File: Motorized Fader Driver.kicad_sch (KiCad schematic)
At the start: 5 parts, among them J1 Conn_01x02, U1 DRV8833PWP, U2 RP2040

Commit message: Update PCB
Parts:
- removed U2: RP2040, Package_DFN_QFN:QFN-56-1EP_7x7mm_P0.4mm_EP3.2x3.2mm, symbol MCU_RaspberryPi:RP2040
- J1: footprint (none) -> Connector_PinHeader_2.54mm:PinHeader_1x02_P2.54mm_Vertical
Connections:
- net RP2040/GPIO5: now reaches U1.15 (AIN2)
- net RP2040/GPIO4: now reaches U1.16 (AIN1)
- net RP2040/GPIO6: now reaches R1.1, VR1.T1
- net RP2040/ADC0: now reaches VR1.B2 (WIPER_2)
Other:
- added sheet RP2040 (rp2040.kicad_sch)
- moved on the sheet: J1, R1, U1, VR1

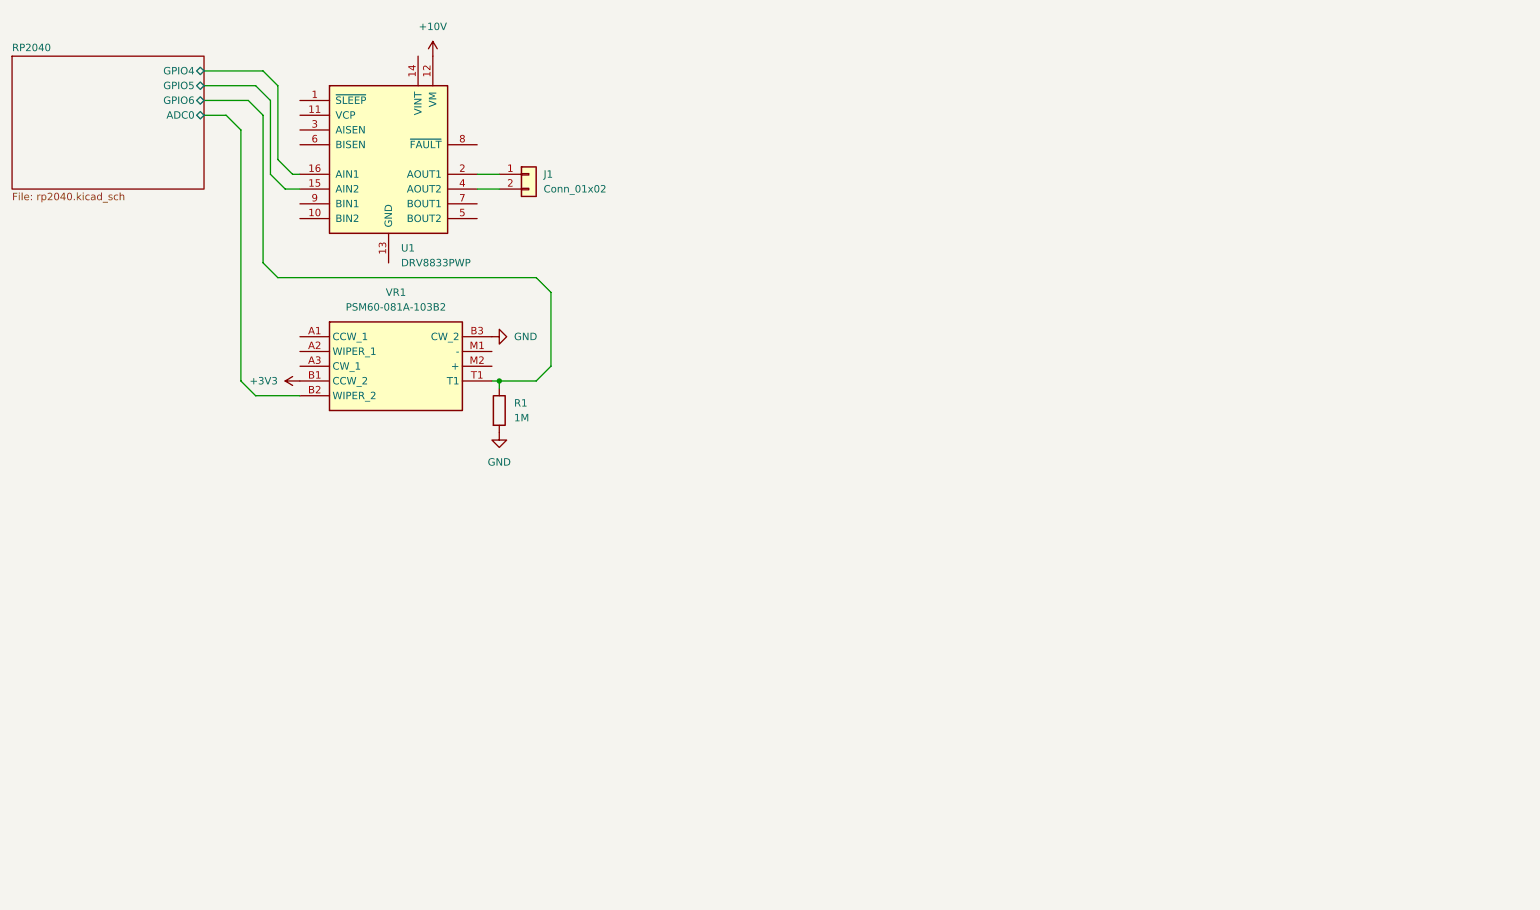
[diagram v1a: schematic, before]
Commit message: Finish most of the schematic design
The majority of the schematic is in a pretty finalized state now. Also
some more work on the PCB has been done.
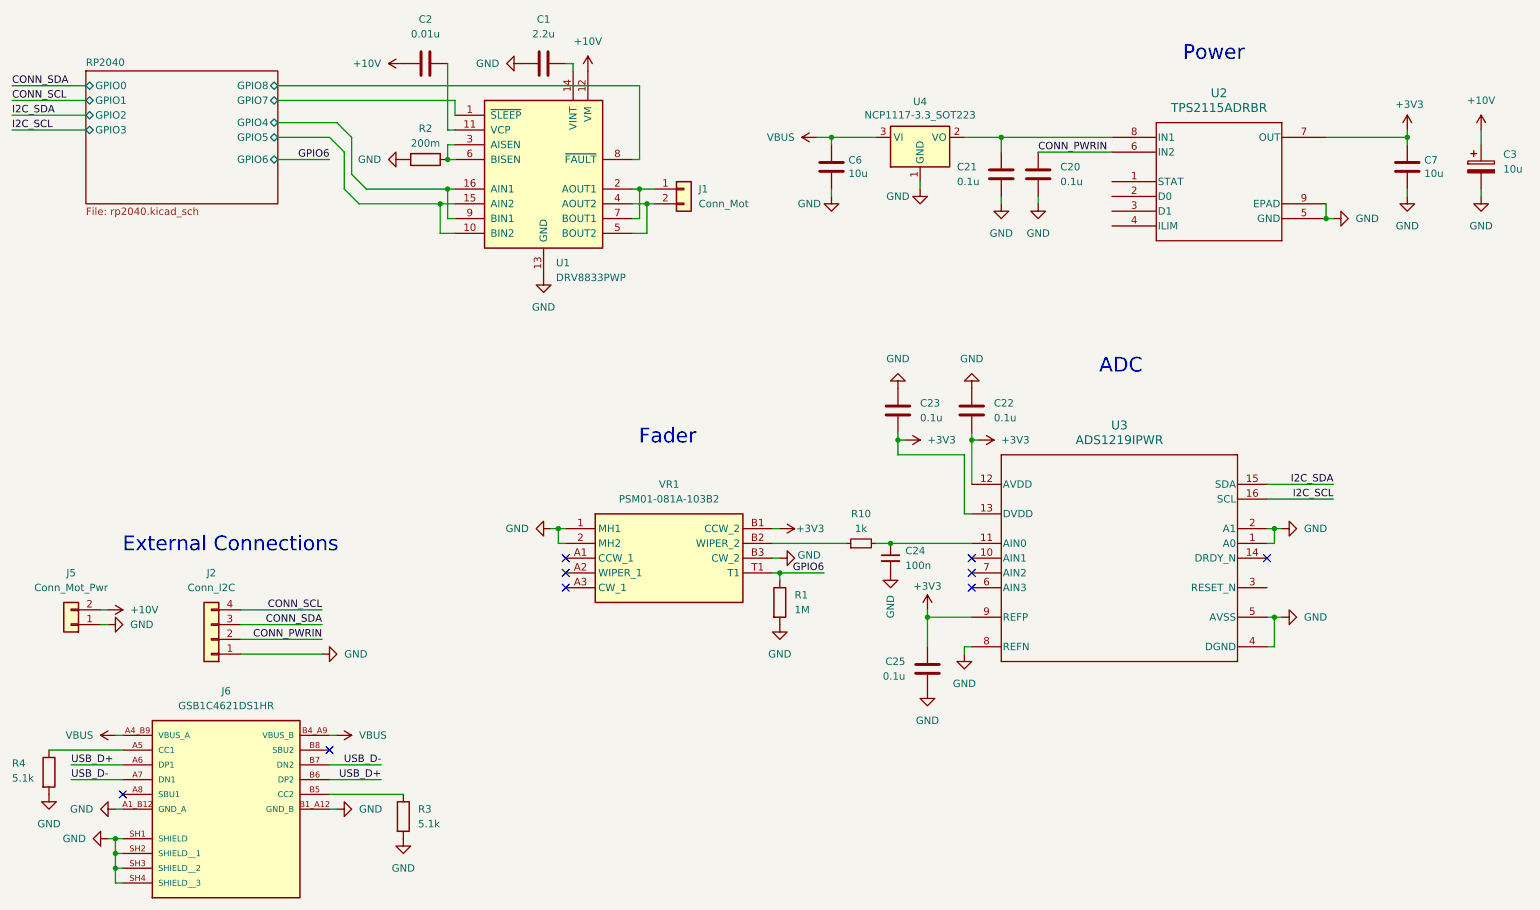
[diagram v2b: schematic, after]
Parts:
- removed VR1: PSM60-081A-103B2, PSM60-081A-103B2:PSM60081A103B2, symbol PSM60-081A-103B2:PSM60-081A-103B2
- added C1: 2.2u, Capacitor_SMD:C_0603_1608Metric, symbol Device:C
- added C2: 0.01u, Capacitor_SMD:C_0603_1608Metric, symbol Device:C
- added C20, C21, C22, C23, C25: 0.1u, Capacitor_SMD:C_0603_1608Metric, symbol Device:C
- added C24: 100n, Capacitor_SMD:C_0603_1608Metric, symbol Device:C_Small
- added C3: 10u, Capacitor_SMD:C_0603_1608Metric, symbol Device:C_Polarized
- added C6, C7: 10u, Capacitor_SMD:C_0603_1608Metric, symbol Device:C
- added J2: Conn_I2C, Connector_SM04B_SRSS_TB:CONN_SM04B-SRSS-TB_JST, symbol Connector_Generic:Conn_01x04
- added J5: Conn_Mot_Pwr, Connector_JST:JST_EH_S2B-EH_1x02_P2.50mm_Horizontal, symbol Connector_Generic:Conn_01x02
- added J6: GSB1C4621DS1HR, GSB1C4621DS1HR:AMPHENOL_GSB1C4621DS1HR, symbol GSB1C4621DS1HR:GSB1C4621DS1HR
- added R10: 1k, Resistor_SMD:R_0603_1608Metric, symbol Device:R_Small
- added R2: 200m, Resistor_SMD:R_0603_1608Metric, symbol Device:R
- added R3, R4: 5.1k, Resistor_SMD:R_0603_1608Metric, symbol Device:R
- added U2: TPS2115ADRBR, TPS2115ADRBR:DRB8_2P4X1P65, symbol TPS2115ADRBR:TPS2115ADRBR
- added U3: ADS1219IPWR, ADS1219IPWR:PW0016A_L, symbol ADS1219IPWR:ADS1219IPWR
- added U4: NCP1117-3.3_SOT223, Package_TO_SOT_SMD:SOT-223-3_TabPin2, symbol Regulator_Linear:NCP1117-3.3_SOT223
- added VR1: PSM01-081A-103B2, PSM01-082A-103B2:PSM01081A103B2, symbol PSM01-081A-103B2:PSM01-081A-103B2
- J1: value Conn_01x02 -> Conn_Mot
- R1: footprint (none) -> Resistor_SMD:R_0603_1608Metric
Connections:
- net +10V: now also C2.1, C3.1, J5.2 (Pin_2)
- net +3V3: now also C22.2, C23.1, C25.1, C7.1, U2.7 (OUT), U3.12 (AVDD), U3.13 (DVDD), U3.9 (REFP), VR1.B1 (CCW_2)
- net GND: now also U1.13 (GND), U1.17 (GND), C1.1, C20.2, C21.2, C22.1, C23.2, C24.2, C25.2, C3.2, C6.2, C7.2, J2.1 (Pin_1), J5.1 (Pin_1), J6.A1_B12 (GND_A), J6.B1_A12 (GND_B), J6.SH1 (SHIELD), J6.SH2 (SHIELD__1), J6.SH3 (SHIELD__2), J6.SH4 (SHIELD__3), R2.2, R3.2, R4.2, U2.5 (GND), U2.9 (EPAD), U3.1 (A0), U3.2 (A1), U3.4 (DGND), U3.5 (AVSS), U3.8 (REFN), U4.1 (GND), VR1.1 (MH1), VR1.2 (MH2), VR1.B3 (CW_2)
- net RP2040/GPIO4: now also U1.9 (BIN1)
- net RP2040/GPIO5: now also U1.10 (BIN2)
- net RP2040/GPIO7: now reaches U1.1 (~{SLEEP})
- net at U1.11 (VCP): now also C2.2
- net at U1.14 (VINT): now also C1.2
- net at J1.1 (Pin_1), U1.2 (AOUT1): now also U1.7 (BOUT1)
- net at U1.3 (AISEN): now also U1.6 (BISEN), R2.1
- net at J1.2 (Pin_2), U1.4 (AOUT2): now also U1.5 (BOUT2)
- net RP2040/GPIO8: now reaches U1.8 (~{FAULT})
- net RP2040/GPIO6 renamed GPIO6
- net GPIO6: now also VR1.T1
- new net: J6.A5 (CC1), R4.1
- new net: C21.1, U2.8 (IN1), U4.2 (VO)
- new net: R10.1, VR1.B2 (WIPER_2)
- new net: C24.1, R10.2, U3.11 (AIN0)
- new net: J6.B5 (CC2), R3.1
- new net CONN_PWRIN: C20.1, J2.2 (Pin_2), U2.6 (IN2)
- new net CONN_SCL: J2.4 (Pin_4)
- new net CONN_SDA: J2.3 (Pin_3)
- new net I2C_SCL: U3.16 (SCL)
- new net I2C_SDA: U3.15 (SDA)
- new net USB_D+: J6.A6 (DP1), J6.B6 (DP2)
- new net USB_D-: J6.A7 (DN1), J6.B7 (DN2)
- new net VBUS: C6.1, J6.A4_B9 (VBUS_A), J6.B4_A9 (VBUS_B), U4.3 (VI)
- no-connect marks 0 -> 9
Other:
- sheet RP2040 ports: added GPIO0, GPIO1, GPIO2, GPIO3, GPIO7, GPIO8; removed ADC0
- note added: "ADC"
- note added: "External Connections"
- note added: "Fader"
- note added: "Power"
- moved on the sheet: J1, R1, U1

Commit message: Finish routing most of the PCB
The PCB should work now for the most part. Also fixes some miscellaneous
schematic things and swaps out a few components.
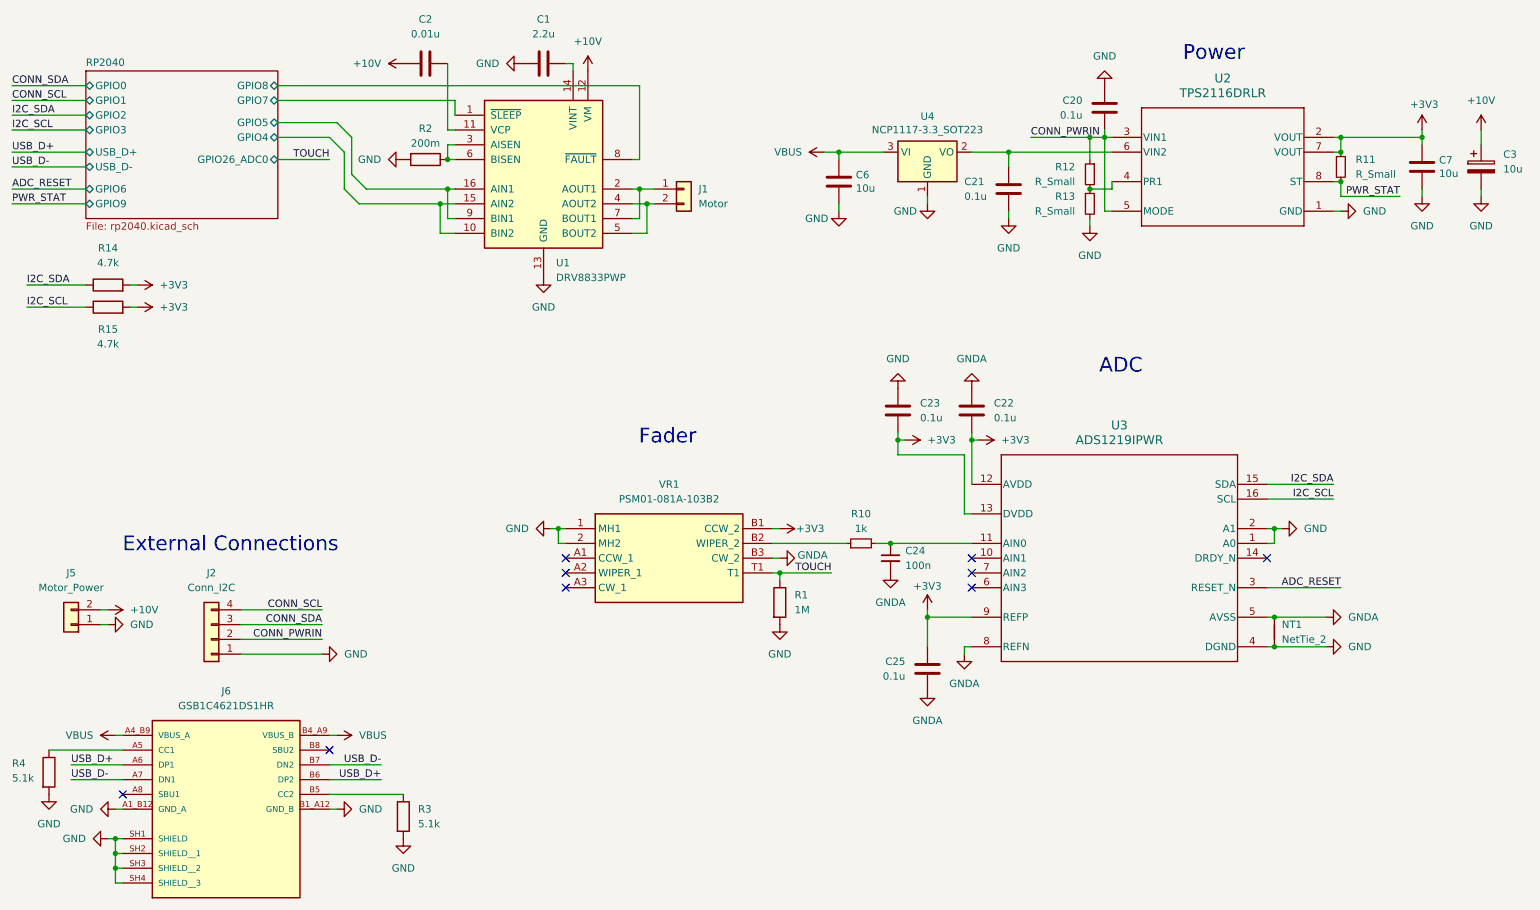
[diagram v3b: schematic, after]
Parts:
- removed U2: TPS2115ADRBR, TPS2115ADRBR:DRB8_2P4X1P65, symbol TPS2115ADRBR:TPS2115ADRBR
- added NT1: NetTie_2, NetTie:NetTie-2_SMD_Pad0.5mm, symbol Device:NetTie_2
- added R11, R12, R13: R_Small, Resistor_SMD:R_0603_1608Metric, symbol Device:R_Small
- added R14, R15: 4.7k, Resistor_SMD:R_0603_1608Metric, symbol Device:R
- added U2: TPS2116DRLR, TPS2116DRLR:DRL0008A-MFG, symbol TPS2116DRLR:TPS2116DRLR
- J1: value Conn_Mot -> Motor
- J5: value Conn_Mot_Pwr -> Motor_Power
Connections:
- net +3V3: now also R11.1, R14.2, R15.2, U2.2 (VOUT), U2.7 (VOUT)
- net CONN_PWRIN: now also R12.1, U2.3 (VIN1), U2.5 (MODE)
- net GND: now also NT1.1, R13.2, U2.1 (GND); no longer C22.1, C24.2, C25.2, U3.5 (AVSS), U3.8 (REFN), VR1.B3 (CW_2)
- net I2C_SCL: now also R15.1
- net I2C_SDA: now also R14.1
- net RP2040/GPIO4: now also U1.10 (BIN2), U1.15 (AIN2); no longer U1.16 (AIN1), U1.9 (BIN1)
- net RP2040/GPIO5: now also U1.16 (AIN1), U1.9 (BIN1); no longer U1.10 (BIN2), U1.15 (AIN2)
- net at C21.1, U4.2 (VO): now also U2.6 (VIN2)
- net ADC_RESET: now reaches U3.3 (RESET_N)
- net GPIO6 renamed TOUCH
- new net: R12.2, R13.1, U2.4 (PR1)
- new net GNDA: C22.1, C24.2, C25.2, NT1.2, U3.5 (AVSS), U3.8 (REFN), VR1.B3 (CW_2)
- new net PWR_STAT: R11.2, U2.8 (ST)
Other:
- sheet RP2040 ports: added GPIO26_ADC0, GPIO9, USB_D+, USB_D-; removed none
- moved on the sheet: C20, C21, C6, C7, U4

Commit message: Route more things and add LCSC part numbers for things
The LCSC part numbers allow for JLCPCB's PCBA tool to find the parts.
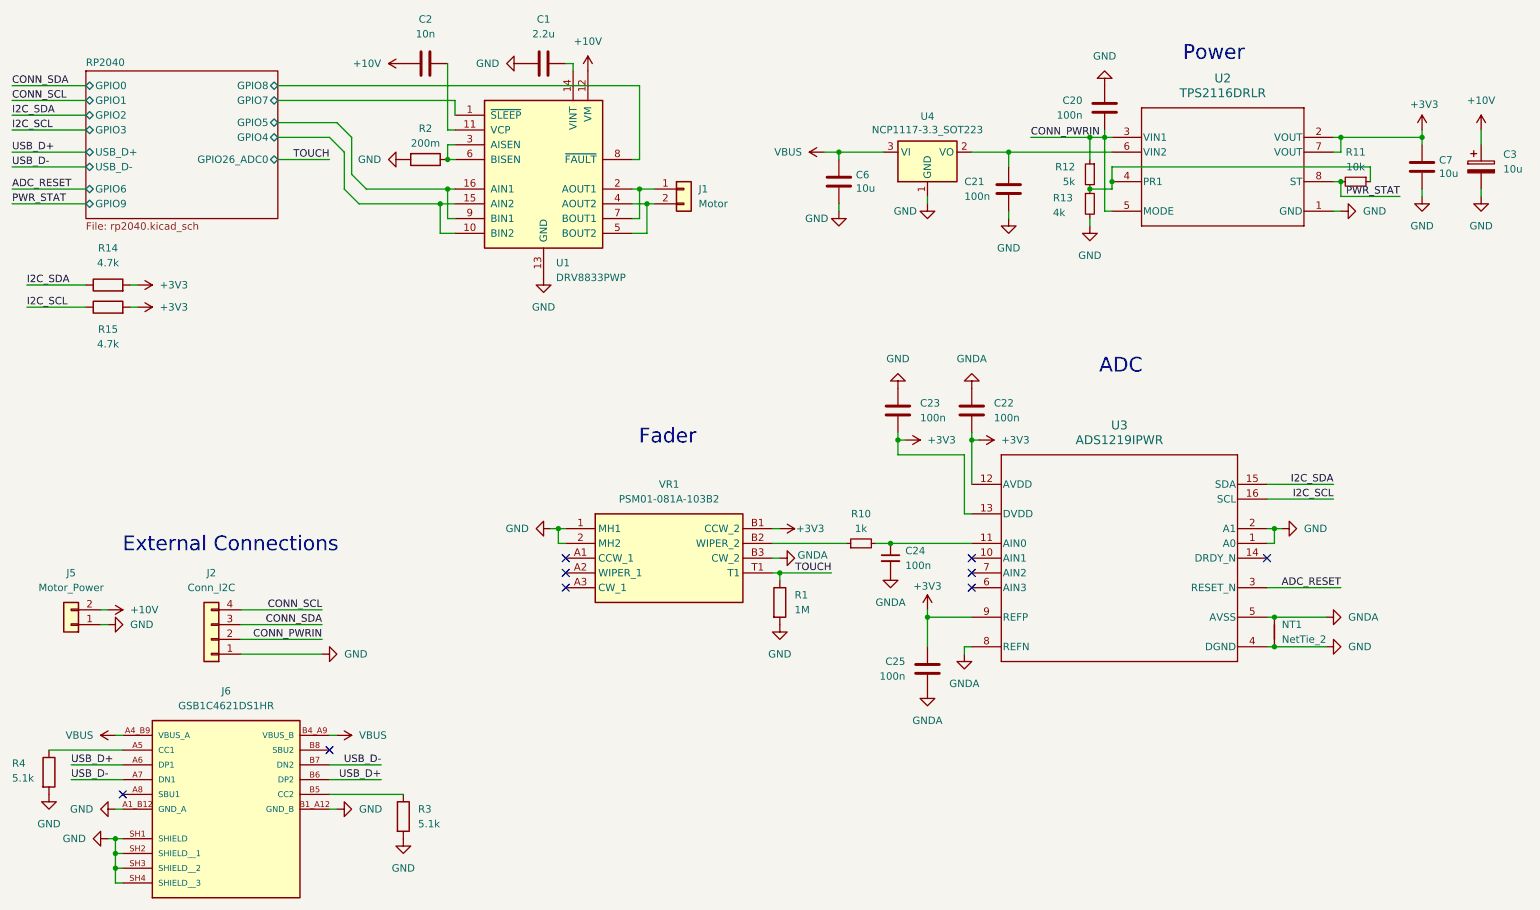
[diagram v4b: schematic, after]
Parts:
- C1: LCSC Part (none) -> C76612
- C2: value 0.01u -> 10n; LCSC Part (none) -> C445735
- C20, C21, C22, C23, C25: value 0.1u -> 100n; LCSC Part (none) -> C76711
- C24: LCSC Part (none) -> C76711
- C3: LCSC Part (none) -> C178496
- C6, C7: LCSC Part (none) -> C76609
- J2: LCSC Part (none) -> C160404
- J5: LCSC Part (none) -> C514173
- J6: LCSC Part (none) -> C20657289
- R1: LCSC Part (none) -> C2907003
- R10: LCSC Part (none) -> C21190
- R11: value R_Small -> 10k; LCSC Part (none) -> C98220
- R12: value R_Small -> 5k; LCSC Part (none) -> C166926
- R13: value R_Small -> 4k; LCSC Part (none) -> C2984443
- R14, R15: LCSC Part (none) -> C99782
- R2: LCSC Part (none) -> C79773
- R3, R4: LCSC Part (none) -> C2907044
- U1: LCSC Part (none) -> C1556089
- U2: LCSC Part (none) -> C3235557
- U3: LCSC Part (none) -> C2869313
- U4: LCSC Part (none) -> C146799
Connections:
- net +3V3: no longer R11.1
- net at R12.2, R13.1, U2.4 (PR1): now also R11.1
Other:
- moved on the sheet: R11

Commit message: Add a debug connector to the schematic
Adds a Paw-Connect debug connector. Not sure if its actually hooked up
yet, since its been a while since I've touched this project and I don't
have KiCad on this computer, but it at least exists in the schematic.
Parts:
- added J3: TC2030, Paw-Connect:Paw-Connect_RevB_TC2030-IDC-NL_2x03_P1.27mm_Vertical, symbol Connector:TC2030
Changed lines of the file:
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@@
+	)
+	(symbol
+		(lib_id "Connector:TC2030")
+		(at 90.17 119.38 0)
+		(unit 1)
+		(exclude_from_sim no)
+		(in_bom no)
+		(on_board yes)
+		(dnp no)
+		(fields_autoplaced yes)
+		(property "Reference" "J3"
+			(at 91.44 106.68 0)
+			(effects
+				(font
+					(size 1.27 1.27)
+				)
+			)
+		)
+		(property "Value" "TC2030"
+			(at 91.44 109.22 0)
+			(effects
+				(font
+					(size 1.27 1.27)
+				)
+			)
+		)
+		(property "Footprint" "Paw-Connect:Paw-Connect_RevB_TC2030-IDC-NL_2x03_P1.27mm_Vertical"
+			(at 91.44 119.38 0)
+			(effects
+				(font
+					(size 1.27 1.27)
+				)
+				(hide yes)
+			)
+		)
+		(property "Datasheet" "https://www.tag-connect.com/wp-content/uploads/bsk-pdf-manager/2019/12/TC2030-IDC-NL-Datasheet-Rev-B.pdf"
+			(at 91.44 119.38 0)
+			(effects
+				(font
+					(size 1.27 1.27)
+				)
+				(hide yes)
+			)
+		)
+		(property "Description" "Tag-Connect’s 6-pins connector"
+			(at 90.17 119.38 0)
+			(effects
+				(font
+					(size 1.27 1.27)
+				)
+				(hide yes)
+			)
+		)
+		(pin "6"
+		)
+		(pin "4"
+		)
+		(pin "3"
+		)
+		(pin "5"
+		)
+		(pin "2"
+		)
+		(pin "1"
+		)
+		(instances
+			(project ""
+				(path "/bf621d61-5d08-4d1e-8172-14fa0e2cb1c4"
+					(reference "J3")
+					(unit 1)
+				)
+			)
+		)
 	)
 	(symbol
